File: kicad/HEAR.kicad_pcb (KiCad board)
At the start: 2 copper layers, 39.3 x 106.5 mm, 56 parts, among them J1 PJ341, J12 Euro power header, J13 PJ341, J14 PJ341, J2 PJ341, J3 PJ341, J4 PJ341, J5 Attenuator Jumper 1, J6 Attenuator Jumper 2, U1 TL074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

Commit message: reloaded footprints
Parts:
- J1, J13, J14, J2, J3, J4: footprint Crows:PJ341 -> Crows:PJ341_3.5mm_headphone
- RV2, RV3, RV4, RV5, RV6, RV7, RV8, RV9: footprint Crows:RotaryPotVerticalSingle9mm -> Crows:Potentiometer_Rotary_9mm_Vertical_Single

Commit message: v3 gerbers (had to swap out a cap, part no longer available
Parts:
- C5, C6: footprint Capacitor_SMD:C_0805_2012Metric_Pad1.18x1.45mm_HandSolder -> Capacitor_SMD:C_1206_3216Metric_Pad1.33x1.80mm_HandSolder
- moved C6 0.53 mm to (4.90, 74.9)
- moved C5 0.45 mm to (16.9, 74.4)
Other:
- board text added: "HEAR v3 by Crows Electromusic"
- board text removed: "HEAR by Crows Electromusic"

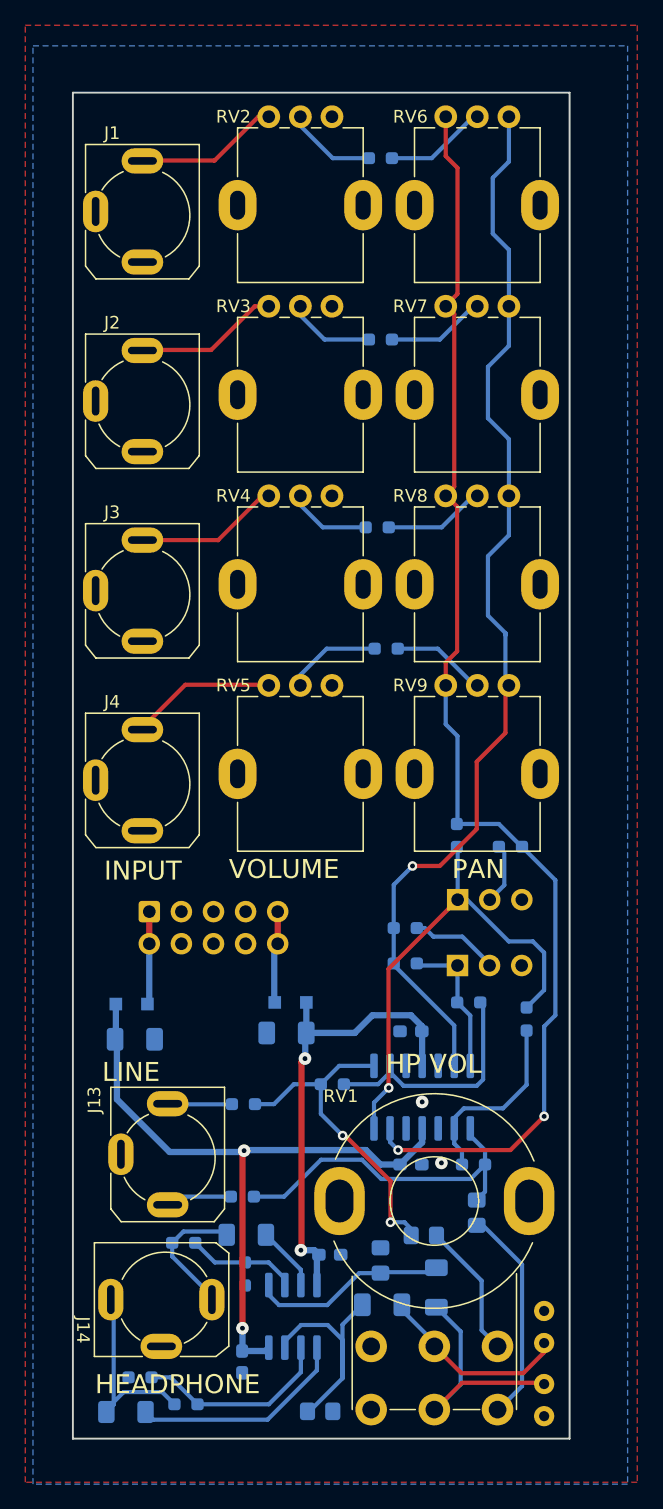
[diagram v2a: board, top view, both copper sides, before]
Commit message: Fix pj341 footprint, tidy up spacing of things
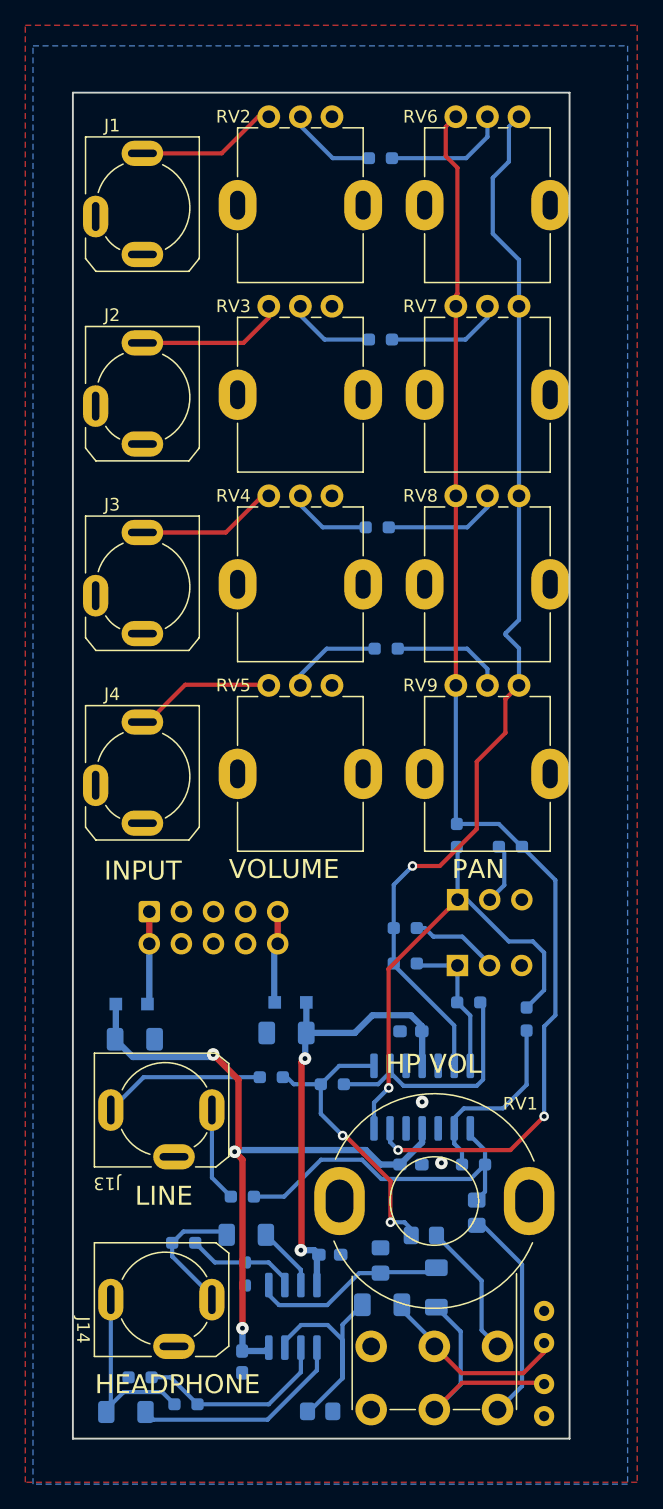
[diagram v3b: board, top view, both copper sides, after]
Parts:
- moved J13 3.54 mm to (7.00, 80.5), turned to -90 degrees
- moved R29 3.07 mm to (15.7, 77.9)
- moved RV6 0.80 mm to (30.3, 1.90)
- moved RV7 0.80 mm to (30.3, 16.9)
- moved RV8 0.80 mm to (30.3, 31.9)
- moved RV9 0.80 mm to (30.3, 46.9)
- moved J3 0.60 mm to (5.50, 38.8)
- moved J4 0.60 mm to (5.50, 53.8)
- moved J1 0.60 mm to (5.50, 8.80)
- moved J2 0.60 mm to (5.50, 23.8)
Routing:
- net LLineOut: track 5.11 -> 12.9 mm
- net Lout: track 26.4 -> 23.7 mm
- net RLineOut: track 5.27 -> 7.47 mm
- net -12V: track 54.0 -> 55.8 mm, vias 2 -> 3
- net Net-(R1-Pad2): track 8.22 -> 9.94 mm
- net /RightMix: track 101.8 -> 100.2 mm
- net Net-(R7-Pad2): track 7.57 -> 9.15 mm
- net Net-(R3-Pad2): track 7.87 -> 9.25 mm
- net Net-(R5-Pad2): track 8.15 -> 9.46 mm
- net /LeftMix: track 85.7 -> 84.8 mm

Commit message: tweak stereo pot footprint
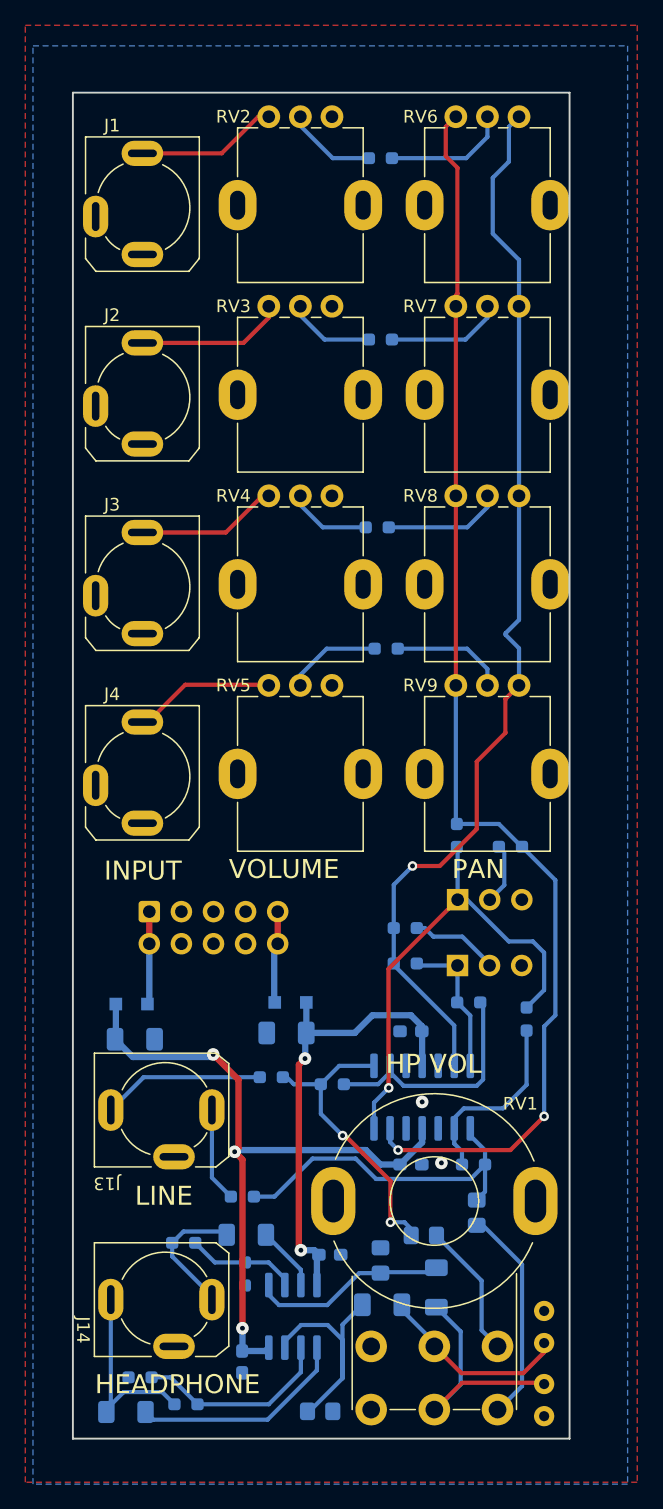
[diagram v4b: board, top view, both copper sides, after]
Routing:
- net -12V: track 55.8 -> 55.0 mm
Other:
- board text added: "HEAR v4 by Crows Electromusic"
- board text removed: "HEAR v3 by Crows Electromusic"
